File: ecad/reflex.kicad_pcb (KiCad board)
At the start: 2 copper layers, 20 x 55 mm, 26 parts, among them J1 USB_MICRO_B_SMD_2, J2 CONN_02X04_RA, Q1 BPW85C, SW1 CHERRY_MX1A-E1NW_BLUE, SW2 B3U-3000P_SPST-NO_SMD, U1 USBLC6, U2 ATSAMD21E18A, U3 AP2112K-3.3, U4 APA102-2020, U5 APA102-2020, X1 SWD_SMT_SOCKET

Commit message: Adds gerber exports
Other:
- board text added: "Board Stackup 55x20 mm 1.6mm or 2.0mm thick FR4 2 layer, 35um (1 oz) copper ENIG or HASL finish OK Green soldermask White silkscreen"
- board text removed: "Board Stackup 55x20 mm 1.6mm or 2.0mm thick FR4 2 layer, 35um (1 oz) copper ENIG or HASL finish OK"
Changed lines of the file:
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@@
     (visible_elements FFFFFF7F)
     (pcbplotparams
-      (layerselection 0x010fc_ffffffff)
-      (usegerberextensions false)
+      (layerselection 0x213f0_ffffffff)
+      (usegerberextensions true)
       (usegerberattributes false)
       (usegerberadvancedattributes false)
@@
       (outputformat 1)
       (mirror false)
-      (drillshape 1)
+      (drillshape 0)
       (scaleselection 1)
-      (outputdirectory ""))
+      (outputdirectory "outputs/"))
   )
   (net 0 "")
@@
     )
   )
-  (gr_text "Board Stackup\n\n55x20 mm\n1.6mm or 2.0mm thick FR4\n2 layer, 35um (1 oz) copper\nENIG or HASL finish OK\n" (at 135.8 96) (layer Cmts.User)
+  (gr_text "Board Stackup\n\n55x20 mm\n1.6mm or 2.0mm thick FR4\n2 layer, 35um (1 oz) copper\nENIG or HASL finish OK\n\nGreen soldermask\nWhite silkscreen" (at 135.8 96) (layer Cmts.User)
     (effects (font (size 3 3) (thickness 0.3)) (justify left))
   )
@@
     (polygon
       (pts
-        (xy 90 130) (xy 104 130) (xy 110.9 123.9) (xy 110.9 73) (xy 90 72.9)
+        (xy 90 130) (xy 104 130) (xy 110.9 123.9) (xy 110.75 75.05) (xy 89.85 74.95)
       )
     )

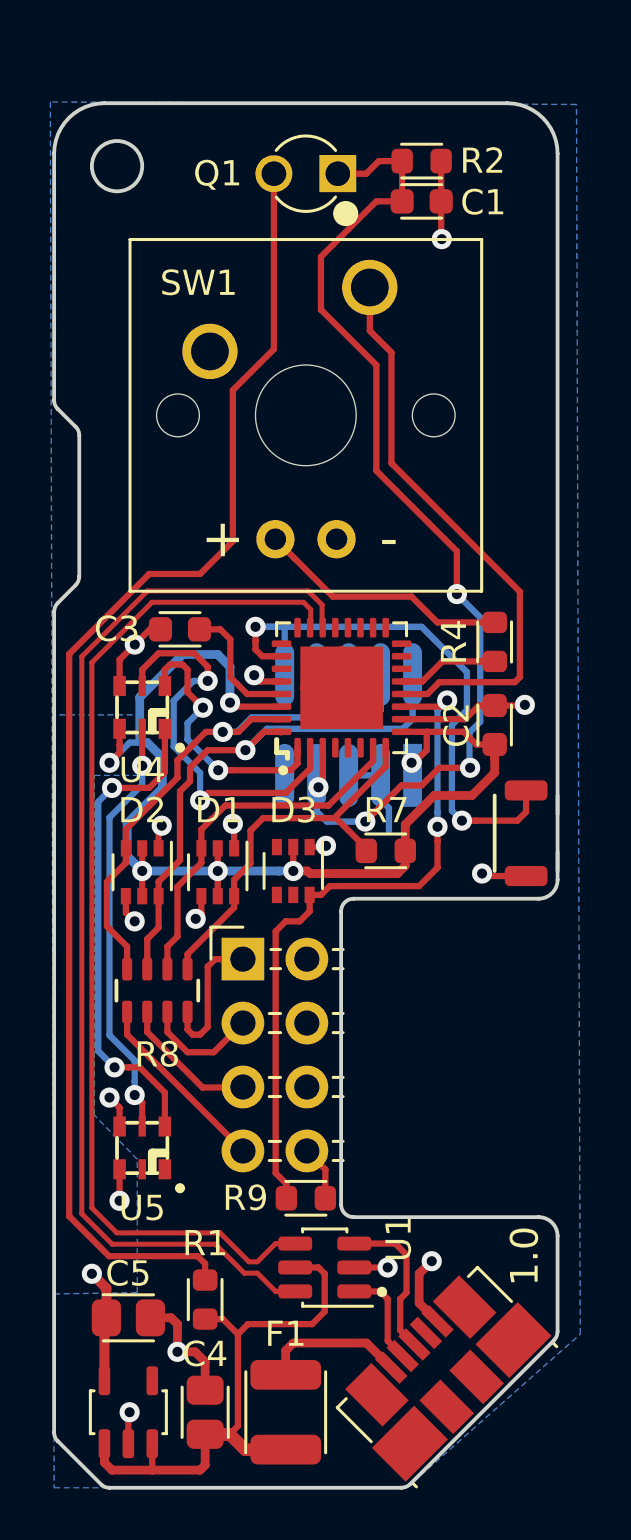
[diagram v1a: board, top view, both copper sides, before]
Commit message: Fixed incorrect USB pinout to microcontroller
Caught with prototype boards :(
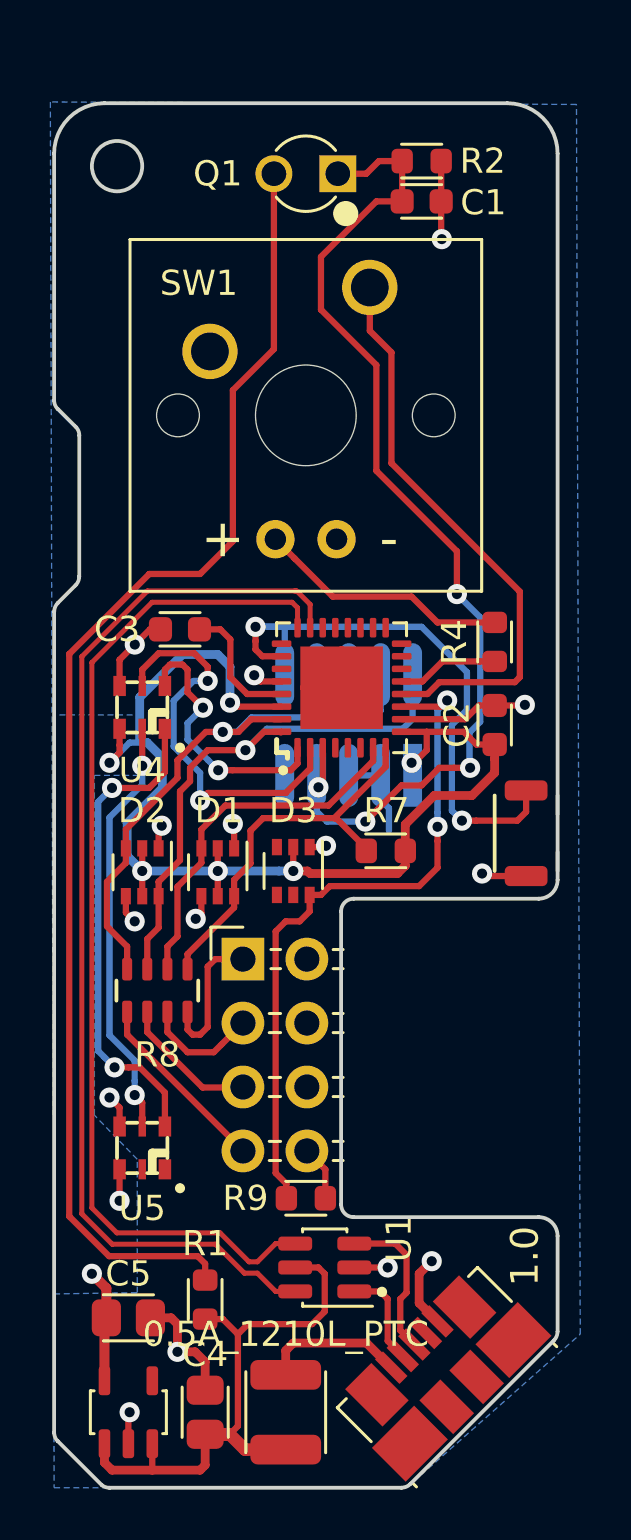
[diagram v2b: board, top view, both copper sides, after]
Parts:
- F1: value F1 -> 0.5A_1210L_PTC
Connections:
- U2 pad 22: USB_D- -> Net-(U2-Pad22)
- U2 pad 23: USB_D+ -> USB_D-
- U2 pad 24: Net-(U2-Pad24) -> USB_D+
- X1 pad 7: PHOTO_TRANS -> Net-(X1-Pad7)
